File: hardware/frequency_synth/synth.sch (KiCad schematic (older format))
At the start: 77 parts

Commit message: finished initial schematic of synth module
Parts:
- removed C?: 100 nF, Capacitors_SMD:C_0402, symbol C_Small
- removed R?: R_Small, Resistors_SMD:R_0402, symbol R_Small
- removed U?: TXCO, vna_footprints:crystal_FA238-TSX3225, symbol TXCO
- added R?: 68, Resistors_SMD:R_0402, symbol R_Small
- added R?: 0, Resistors_SMD:R_0402, symbol R_Small
- R4: renamed from R?; value DNP -> 68
- R5: renamed from R?; value 0 -> 18
- R6: renamed from R?; value 1k -> 18
- gave numbers to parts that had none: 71
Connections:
- net labels added: LMX_REFIN_N, LMX_REFIN_P
- wire segments 218 -> 211

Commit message: reducing component values across module, synth schematic cleanups
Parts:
- removed C1, C32, C34, C40: 100 nF, Capacitors_SMD:C_0402, symbol C_Small
- removed C2: 10 uF, Capacitors_SMD:C_0603, symbol CP_Small
- removed U1, U4, U5: CONN_SMA, vna_footprints:732512200_SMA, symbol CONN_SMA
- added U? (x3): CONN_SMA_2GND, symbol CONN_SMA_2GND
- C31, C33: value 30 pF -> 10 pF
- C39: value 30 pF -> 100 pF
- L1: footprint (none) -> Resistors_SMD:R_0603
- L2, L3: value 18 nF -> 5.6 nF
- gave numbers to parts that had none: 2
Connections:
- wire segments 211 -> 182
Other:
- moved on the sheet: C31, C33, C39

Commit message: started on component placement
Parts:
- removed D2: LED, LEDs:LED_0603, symbol LED
- removed R8: 1k, Resistors_SMD:R_0402, symbol R_Small
- L201: renamed from L1; value INDUCTOR_SMALL -> FERRITE CHIP
- U201, U203, U204: renamed from U?; footprint (none) -> vna_footprints:734120110_ufl_umc
- renumbered C3 to C201, C4 to C202, C5 to C203, C6 to C204, C7 to C205, C8 to C206, C10 to C207, C11 to C208, C12 to C209, C13 to C210, C14 to C211, C15 to C212, C16 to C213, C17 to C214, C18 to C215, C19 to C216, C20 to C217, C21 to C218, C22 to C219, C23 to C220, C24 to C221, C25 to C222, C26 to C223, C27 to C224, C28 to C225, C29 to C226, C30 to C227, C31 to C228, C33 to C229, C35 to C230, C36 to C231, C37 to C232, C38 to C233, C39 to C234, D1 to D201, L2 to L202, L3 to L203, R2 to R201, R3 to R202, R1 to R203, R52 to R204, R4 to R205, R5 to R206, R6 to R207, R7 to R208, R9 to R209, R10 to R210, R11 to R211, R12 to R212, R13 to R213, R14 to R214, R15 to R215, R16 to R216, R17 to R217, R18 to R218, R19 to R219, R20 to R220, R21 to R221, R22 to R222, R23 to R223, R24 to R224, R25 to R225, R26 to R226, R27 to R227, U3 to U202

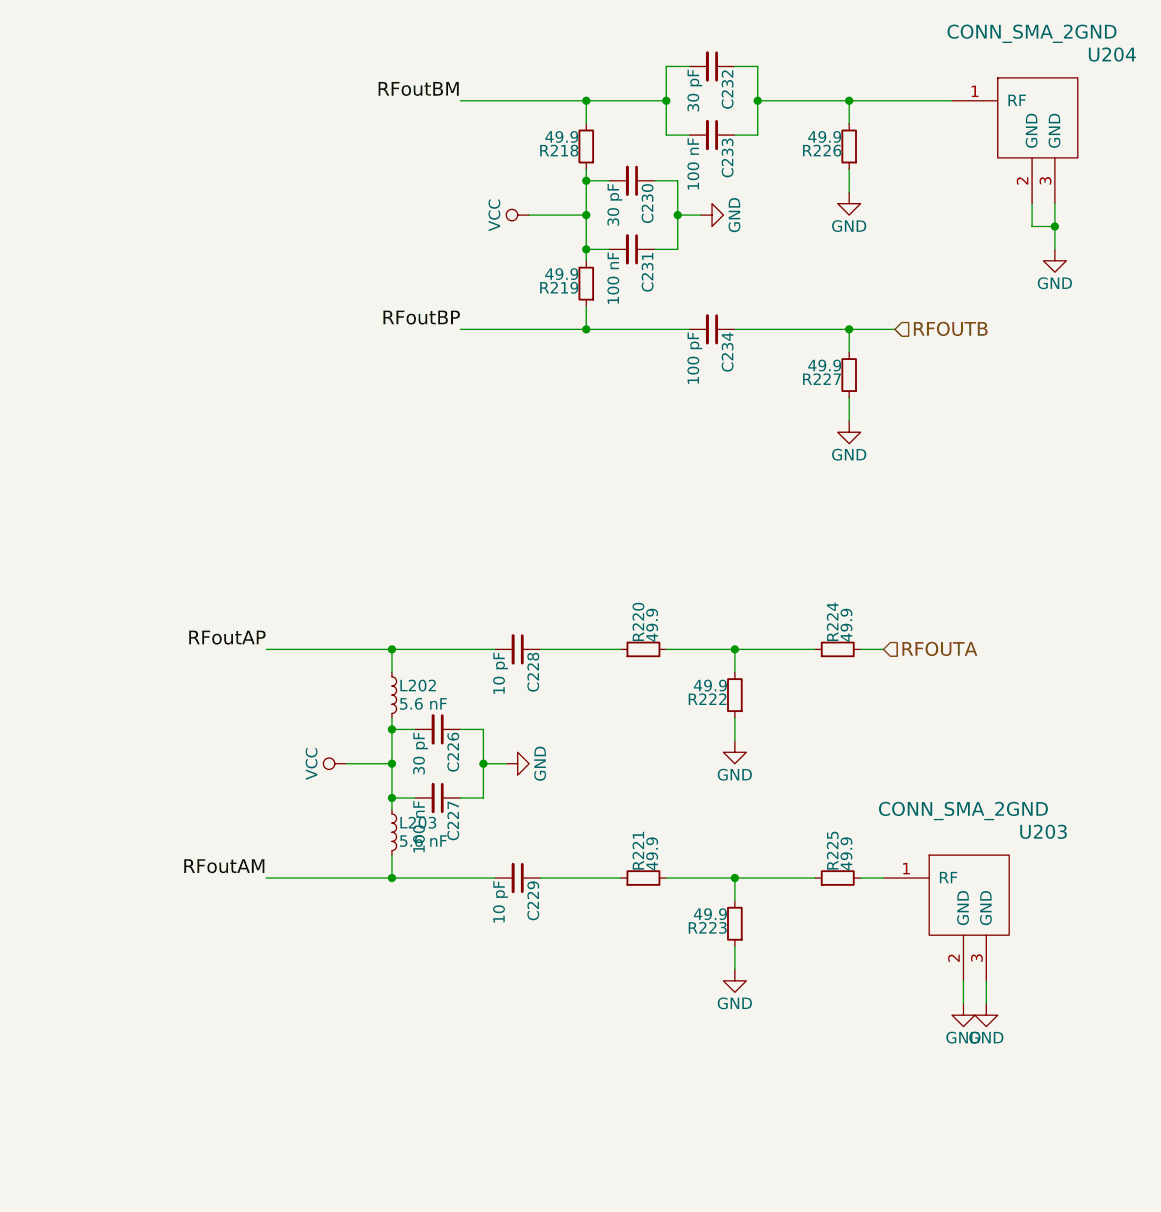
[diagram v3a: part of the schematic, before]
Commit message: added sma edge launch cutout SLOT cal board
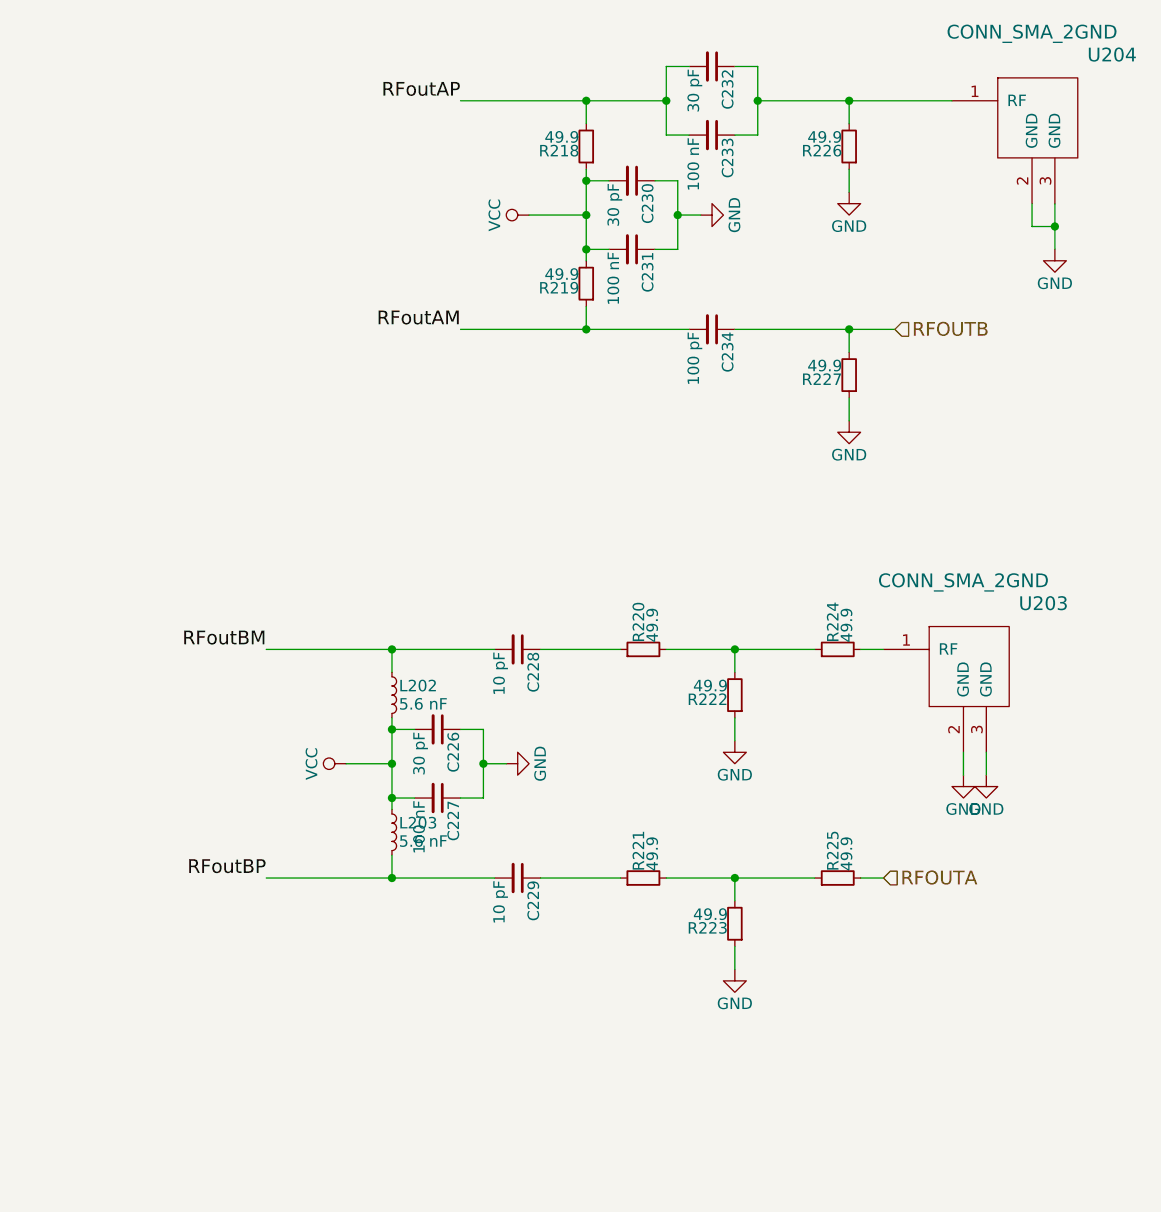
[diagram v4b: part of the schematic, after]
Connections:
- net RFOUTA: now also R225.2; no longer R224.2
- net RFoutAM: now also C234.2, R219.1; no longer C229.2, L203.2
- net RFoutAP: now also C232.2, C233.2, R218.2; no longer C228.2, L202.1
- net RFoutBM: now also C228.2, L202.1; no longer C232.2, C233.2, R218.2
- net RFoutBP: now also C229.2, L203.2; no longer C234.2, R219.1
- net at U203.1 (RF): now also R224.2; no longer R225.2
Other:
- moved on the sheet: U203
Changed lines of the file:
@@
 Text Label 8750 5600 0    60   ~ 0
 RFoutAM
+Text Label 12000 5050 2    60   ~ 0
+RFoutBP
+Text Label 12000 4050 2    60   ~ 0
+RFoutBM
+Text Label 12850 1650 2    60   ~ 0
+RFoutAP
 Text Label 12850 2650 2    60   ~ 0
-RFoutBP
-Text Label 12850 1650 2    60   ~ 0
-RFoutBM
-Text Label 12000 4050 2    60   ~ 0
-RFoutAP
-Text Label 12000 5050 2    60   ~ 0
 RFoutAM
 Text Label 7800 9800 1    60   ~ 0
@@
 Text HLabel 14750 2650 2    60   Input ~ 0
 RFOUTB
-Text HLabel 14700 4050 2    60   Input ~ 0
+Text HLabel 14700 5050 2    60   Input ~ 0
 RFOUTA
 Text HLabel 7800 10600 3    60   Input ~ 0
@@
 L CONN_SMA_2GND U203
 U 1 1 572CFBDF
-P 15100 5050
-F 0 "U203" H 14800 5250 60  0000 C CNN
-F 1 "CONN_SMA_2GND" H 15150 5350 60  0000 C CNN
-F 2 "vna_footprints:734120110_ufl_umc" H 15100 5050 60  0001 C CNN
-F 3 "" H 15100 5050 60  0000 C CNN
-	1    15100 5050
+P 15100 4050
+F 0 "U203" H 14800 4250 60  0000 C CNN
+F 1 "CONN_SMA_2GND" H 15150 4350 60  0000 C CNN
+F 2 "vna_footprints:734120110_ufl_umc" H 15100 4050 60  0001 C CNN
+F 3 "" H 15100 4050 60  0000 C CNN
+	1    15100 4050
 	-1   0    0    -1
 $EndComp
@@
 L GND #PWR076
 U 1 1 572D0241
-P 15050 5600
-F 0 "#PWR076" H 15050 5350 50  0001 C CNN
-F 1 "GND" H 15050 5450 50  0000 C CNN
-F 2 "" H 15050 5600 50  0000 C CNN
-F 3 "" H 15050 5600 50  0000 C CNN
-	1    15050 5600
+P 15050 4600
+F 0 "#PWR076" H 15050 4350 50  0001 C CNN
+F 1 "GND" H 15050 4450 50  0000 C CNN
+F 2 "" H 15050 4600 50  0000 C CNN
+F 3 "" H 15050 4600 50  0000 C CNN
+	1    15050 4600
 	1    0    0    -1
 $EndComp
@@
 L GND #PWR077
 U 1 1 572D032A
-P 15150 5600
-F 0 "#PWR077" H 15150 5350 50  0001 C CNN
-F 1 "GND" H 15150 5450 50  0000 C CNN
-F 2 "" H 15150 5600 50  0000 C CNN
-F 3 "" H 15150 5600 50  0000 C CNN
-	1    15150 5600
+P 15150 4600
+F 0 "#PWR077" H 15150 4350 50  0001 C CNN
+F 1 "GND" H 15150 4450 50  0000 C CNN
+F 2 "" H 15150 4600 50  0000 C CNN
+F 3 "" H 15150 4600 50  0000 C CNN
+	1    15150 4600
 	1    0    0    -1
 $EndComp
 Wire Wire Line
-	15150 5500 15150 5600
-Wire Wire Line
-	15050 5500 15050 5600
+	15150 4500 15150 4600
+Wire Wire Line
+	15050 4500 15050 4600
 $Comp
 L CONN_SMA_2GND U204

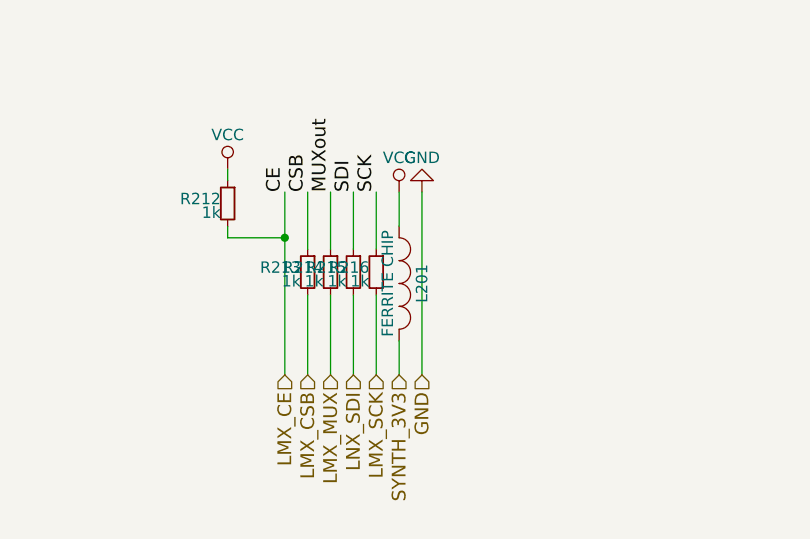
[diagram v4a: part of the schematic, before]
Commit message: work on layout of synth, done up to output stage of lmx2592
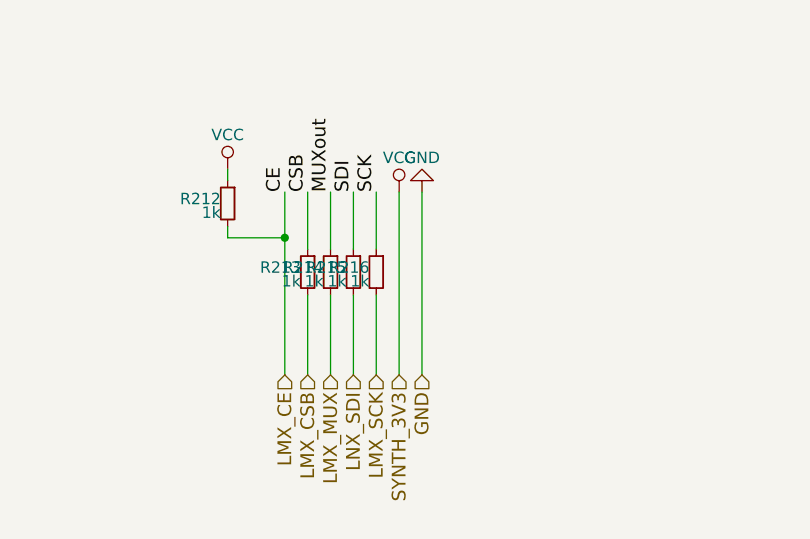
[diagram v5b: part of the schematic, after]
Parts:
- removed L201: FERRITE CHIP, Resistors_SMD:R_0603, symbol INDUCTOR_SMALL
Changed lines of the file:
@@
 Text HLabel 8300 10600 3    60   Input ~ 0
 SYNTH_3V3
-$Comp
-L INDUCTOR_SMALL L201
-U 1 1 572B54BD
-P 8300 10200
-F 0 "L201" H 8300 10300 50  0000 C CNN
-F 1 "FERRITE CHIP" H 8300 10150 50  0000 C CNN
-F 2 "Resistors_SMD:R_0603" H 8300 10200 50  0001 C CNN
-F 3 "" H 8300 10200 50  0000 C CNN
-	1    8300 10200
-	0    1    1    0
-$EndComp
 Wire Wire Line
-	8300 10450 8300 10600
-Wire Wire Line
-	8300 9950 8300 9800
+	8300 9800 8300 10600
 Text HLabel 8400 10600 3    60   Input ~ 0
 GND

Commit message: work on synth board layout..
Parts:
- removed C201, C203, C205: 100 nF, Capacitors_SMD:C_0402, symbol C_Small

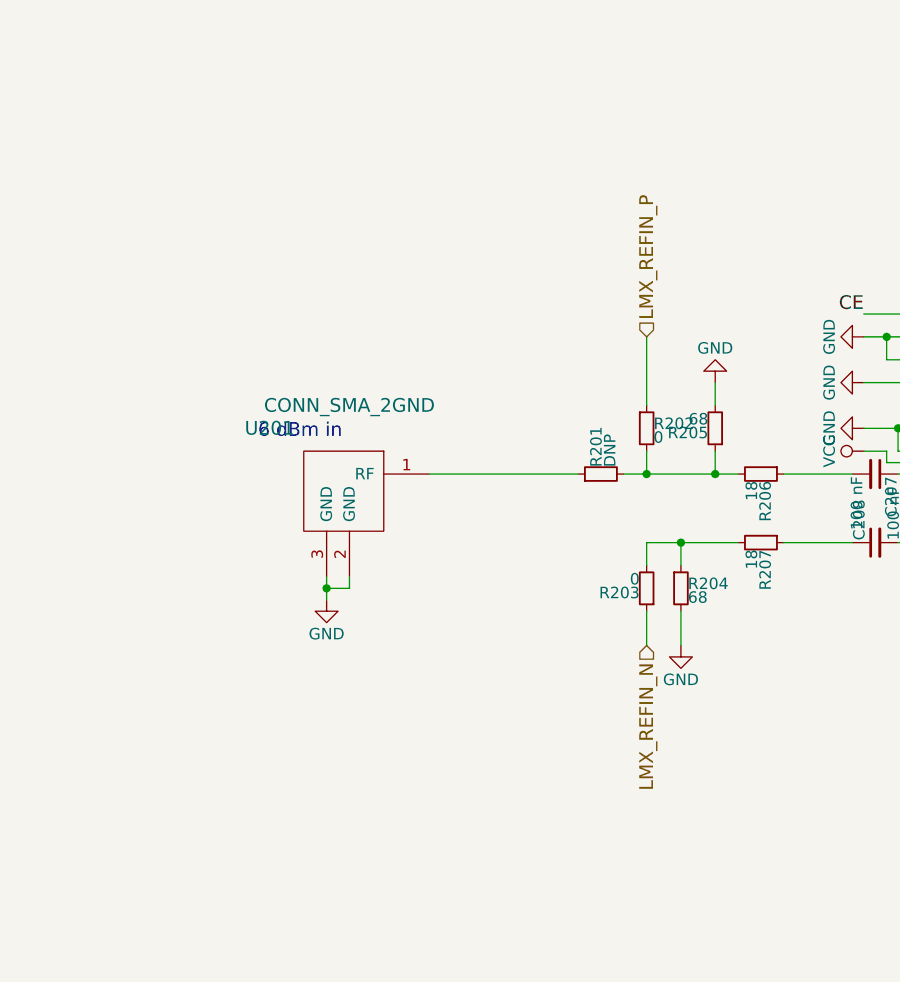
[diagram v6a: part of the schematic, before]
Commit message: all nets connected on synth layout..
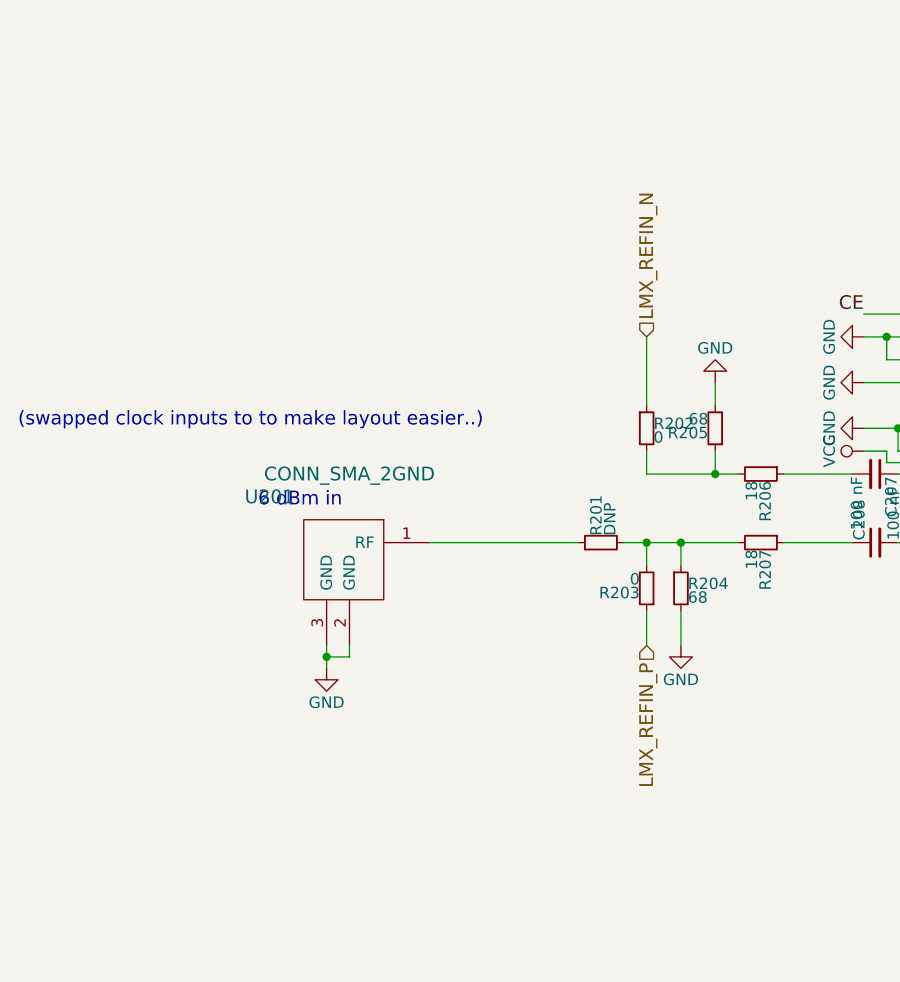
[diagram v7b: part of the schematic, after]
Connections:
- net LMX_REFIN_N: now also R202.1; no longer R203.1
- net LMX_REFIN_P: now also R203.1; no longer R202.1
- net at R202.2, R205.1, R206.2: no longer R201.2
- net at R203.2, R204.1, R207.2: now also R201.2
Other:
- note added: "(swapped clock inputs to to make layout easier..)"
- moved on the sheet: R201, U201

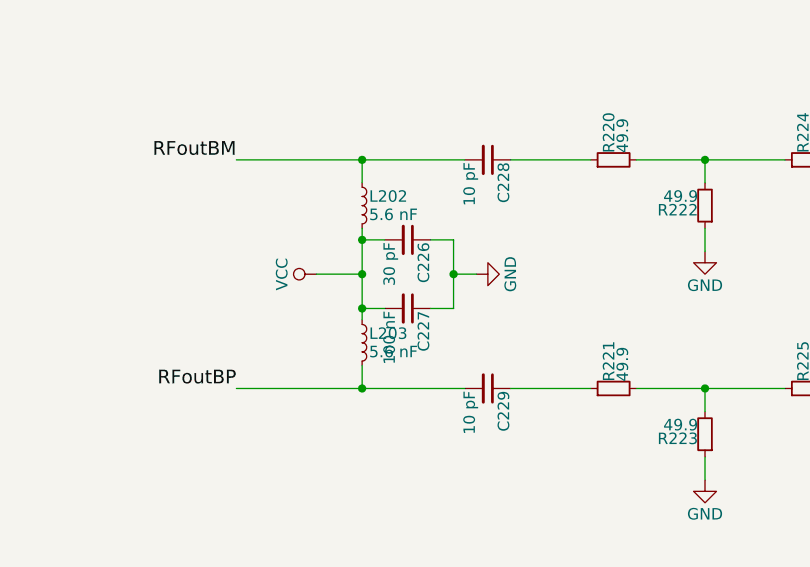
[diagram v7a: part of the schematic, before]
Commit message: added synth BOM, paste stencil
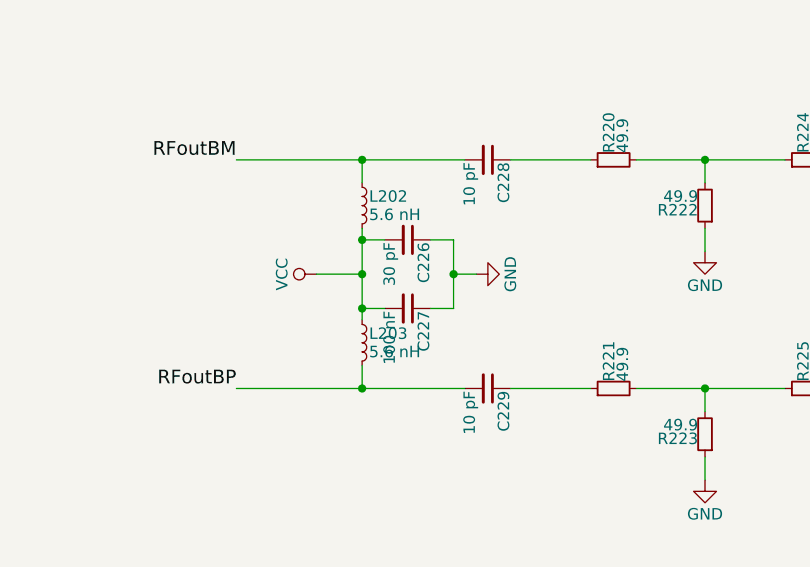
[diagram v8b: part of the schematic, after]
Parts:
- L202, L203: value 5.6 nF -> 5.6 nH
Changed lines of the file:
@@
 P 12550 4250
 F 0 "L202" H 12580 4290 50  0000 L CNN
-F 1 "5.6 nF" H 12580 4210 50  0000 L CNN
+F 1 "5.6 nH" H 12580 4210 50  0000 L CNN
 F 2 "Resistors_SMD:R_0402" H 12550 4250 50  0001 C CNN
 F 3 "" H 12550 4250 50  0000 C CNN
@@
 P 12550 4850
 F 0 "L203" H 12580 4890 50  0000 L CNN
-F 1 "5.6 nF" H 12580 4810 50  0000 L CNN
+F 1 "5.6 nH" H 12580 4810 50  0000 L CNN
 F 2 "Resistors_SMD:R_0402" H 12550 4850 50  0001 C CNN
 F 3 "" H 12550 4850 50  0000 C CNN
